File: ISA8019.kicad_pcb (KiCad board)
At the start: 2 copper layers, 127.5 x 72.1 mm, 52 parts, among them J1 Bus_ISA_8bit, J2 8P8C_Shielded, J4 Jumper mode, J5 PNP force, J6 BROM size and base address, J7 I/O base address, J8 Medium type, J9 IRQ select, T1 13F-39MNL, U1 RTL8019AS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

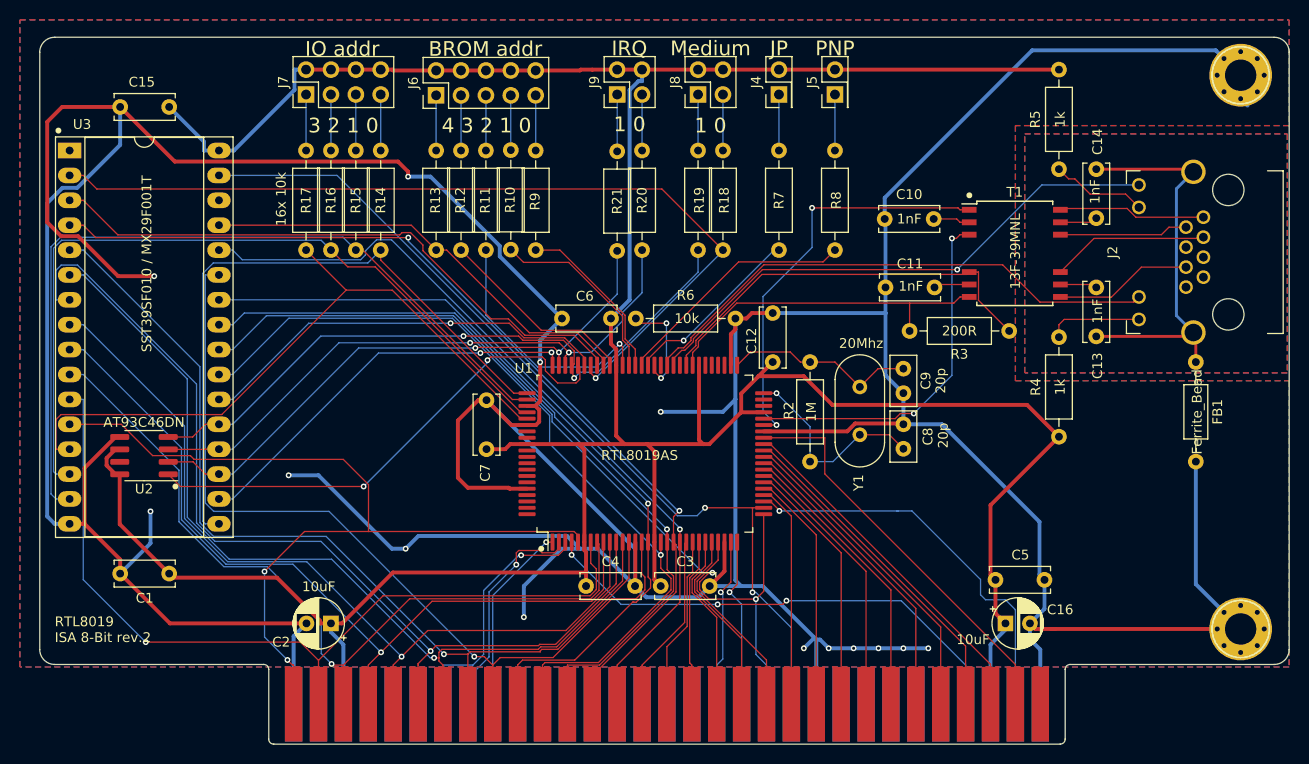
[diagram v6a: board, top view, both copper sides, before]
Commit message: Smaller version of the ethernet card
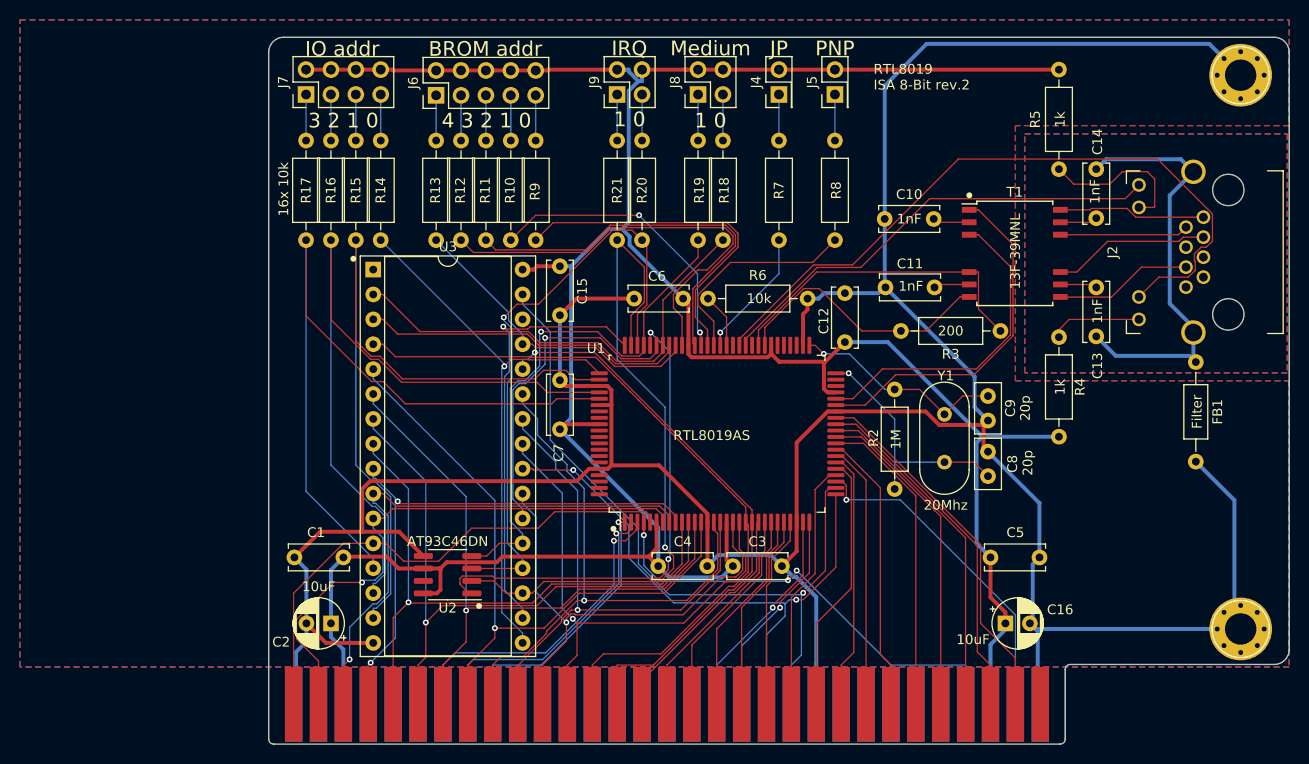
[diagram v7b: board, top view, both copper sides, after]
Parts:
- FB1: value Ferrite_Bead -> Filter
- R3: value 200R -> 200
- U3: footprint Package_DIP:DIP-32_W15.24mm_Socket_LongPads -> Package_DIP:DIP-32_W15.24mm_Socket
- moved C15 43.1 mm to (118.7, 114.6), turned to 270 degrees
- moved U2 33.3 mm to (107.2, 146.1)
- moved U3 33.3 mm to (99.6, 114.9)
- moved C1 17.9 mm to (96.6, 144.3)
- moved C8 9.08 mm to (162.4, 133.5)
- moved C9 9.08 mm to (162.4, 130.3)
- moved R2 9.08 mm to (152.8, 137.3)
- moved Y1 9.08 mm to (157.9, 129.7)
- moved C7 7.76 mm to (118.7, 131.2)
- moved C4 7.64 mm to (128.7, 145.2)
- moved C6 7.64 mm to (131.3, 117.9)
- moved R6 7.64 mm to (133.8, 117.9)
- moved U1 7.64 mm to (134.7, 131.7)
- moved C3 7.64 mm to (136.3, 145.2)
- moved C12 7.64 mm to (147.8, 122.3)
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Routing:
- net GND: track 606.7 -> 364.8 mm, vias 14 -> 0
- net /BA14: track 89.8 -> 46.7 mm, vias 1 -> 0
- net +5V: track 349.3 -> 309.9 mm
- net /ISA_A10: track 84.8 -> 50.2 mm
- net /ISA_A5: track 99.5 -> 65.0 mm
- net /ISA_A0: track 87.2 -> 53.5 mm, vias 2 -> 0
- net /~ISA_SMEMR: track 91.9 -> 59.6 mm
- net /ISA_A1: track 88.1 -> 57.2 mm
- net /ISA_A3: track 84.9 -> 56.1 mm, vias 1 -> 2
- net /ISA_A8: track 88.6 -> 59.8 mm
- net /BA15: track 61.8 -> 33.2 mm
- net /ISA_A7: track 95.6 -> 68.0 mm
- net /ISA_A6: track 93.3 -> 65.8 mm
- net /ISA_A2: track 83.5 -> 56.2 mm
- net /ISA_A9: track 82.1 -> 55.6 mm
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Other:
- board size 127.5 x 72.1 mm -> 104.1 x 72.1 mm
